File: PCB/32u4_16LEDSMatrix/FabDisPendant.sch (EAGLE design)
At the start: 68 parts, among them IC1 MPR121, U1 ATMEGA32U4-AU, Y1 16MHz

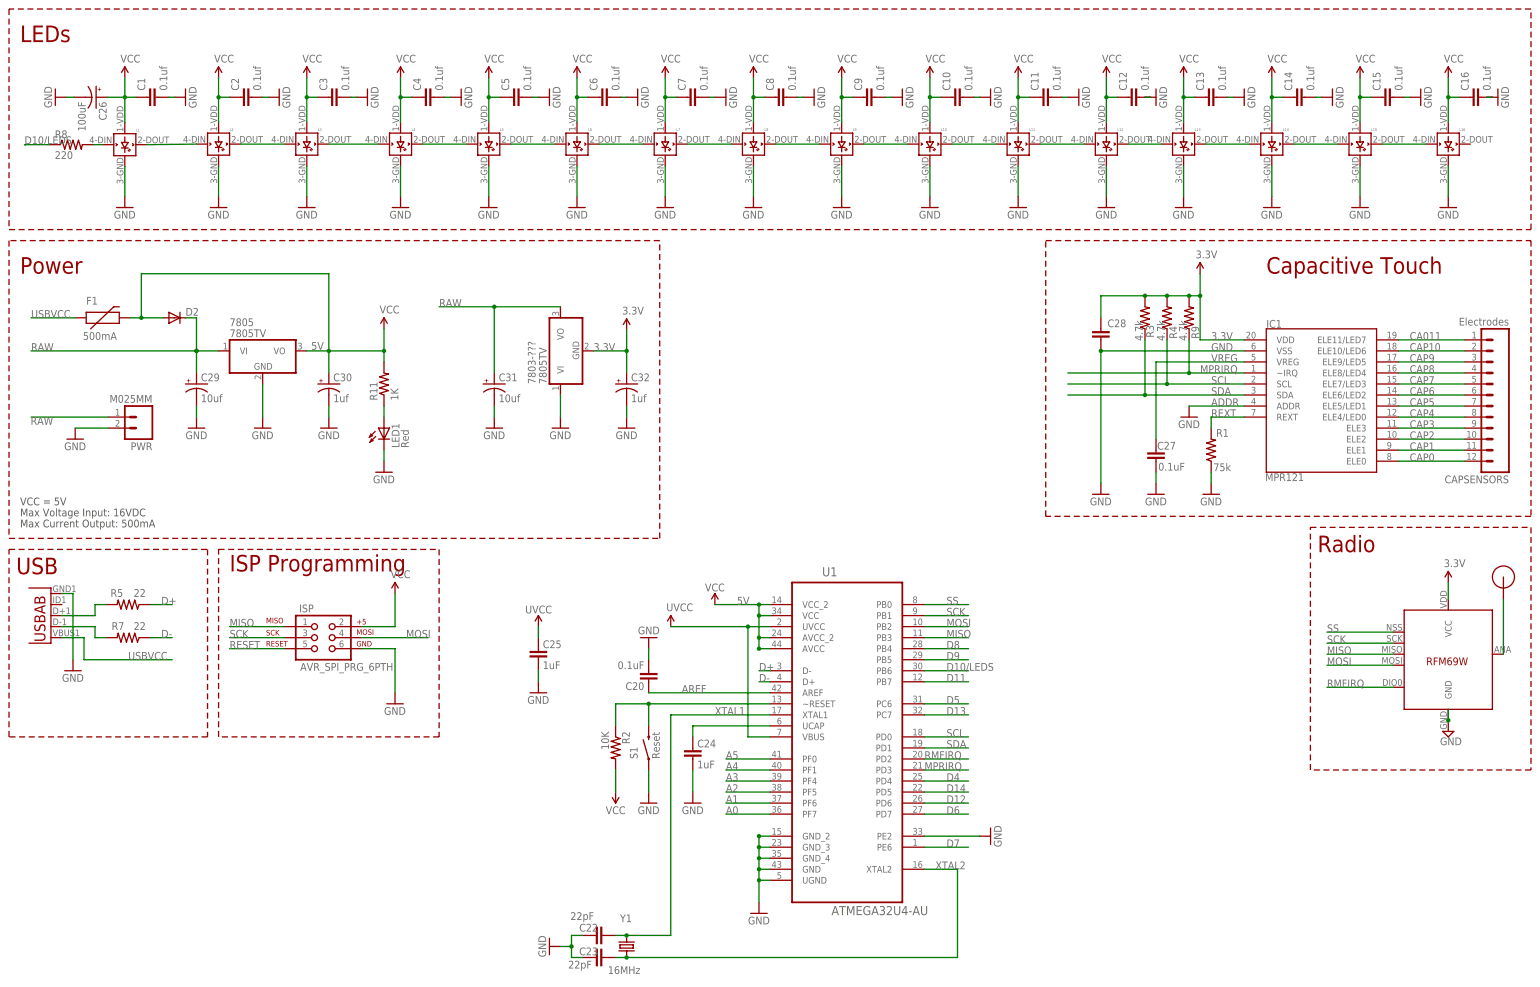
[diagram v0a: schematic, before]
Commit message: Completed switch to using 32u4 with the AU package
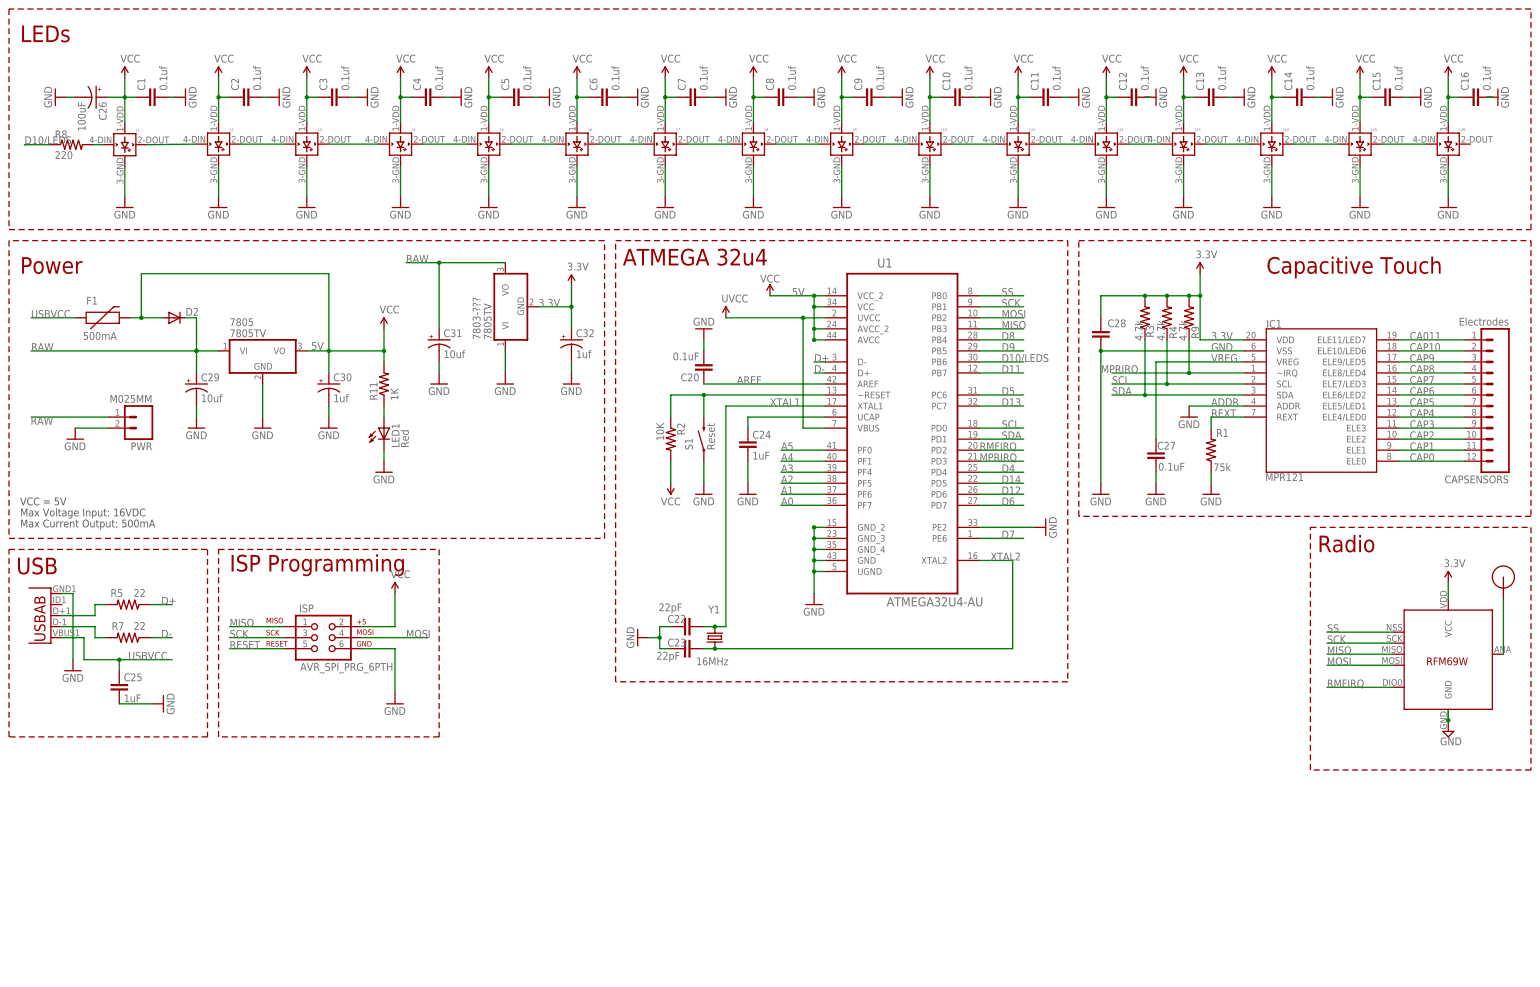
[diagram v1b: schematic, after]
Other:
- note added: "ATMEGA 32u4"
- moved on the sheet: 7803-???, C20, C22, C23, C24, C25, C31, C32, R2, S1, U1, Y1
